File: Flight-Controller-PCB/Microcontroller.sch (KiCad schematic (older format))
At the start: 32 parts, among them J8 USB_B_Micro, J9 ICSP, SW1 Reset, U3 FT232RL, U4 ATmega328P-AU, U5 LM1117-5.0, Y1 16 MHz

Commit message: Deleted majority of unused components. Started schematic for new MCU
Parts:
- removed C10, C11, C18: 0.1uF 16V X7R 10%, Capacitor_SMD:C_0603_1608Metric_Pad1.05x0.95mm_HandSolder, symbol Device:C
- removed D2, D3: Orange 1.9V 20mA, LED_SMD:LED_0603_1608Metric_Pad1.05x0.95mm_HandSolder, symbol Device:LED
- removed D5: Green 2.2V 20mA, LED_SMD:LED_0603_1608Metric_Pad1.05x0.95mm_HandSolder, symbol Device:LED
- removed J9: ICSP, Connector_PinHeader_2.54mm:PinHeader_2x03_P2.54mm_Vertical, symbol Connector_Generic:Conn_02x03_Odd_Even
- removed R16, R17, R22: 200 ohm 5%, Resistor_SMD:R_0603_1608Metric_Pad1.05x0.95mm_HandSolder, symbol Device:R
- removed R21: 1 kohm 5%, Resistor_SMD:R_0603_1608Metric_Pad1.05x0.95mm_HandSolder, symbol Device:R
- removed SW1: Reset, Custom:Switch, symbol Custom:Push-Switch
- removed U3: FT232RL, Package_SO:SSOP-28_5.3x10.2mm_P0.65mm, symbol Interface_USB:FT232RL
- removed U4: ATmega328P-AU, Package_QFP:TQFP-32_7x7mm_P0.8mm, symbol MCU_Microchip_ATmega:ATmega328P-AU
- added R? (x2): 22 ohm 1%, Resistor_SMD:R_0603_1608Metric_Pad1.05x0.95mm_HandSolder, symbol Device:R
- added U?: ATmega32U4-AU, Package_QFP:TQFP-44_10x10mm_P0.8mm, symbol MCU_Microchip_ATmega:ATmega32U4-AU
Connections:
- net labels added: D+, D-
- net labels removed: +3.3V
- wire segments 131 -> 92
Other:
- note removed: "ICSP"
- moved on the sheet: C12, C7, C8, C9, F1, J8, R18, R19, Y1

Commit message: Learned a lot about crystals
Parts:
- added C?: 1uF 16V X7R 10%, Capacitor_SMD:C_0603_1608Metric_Pad1.05x0.95mm_HandSolder, symbol Device:C
- added C? (x2): 22pF 12V X7R 2%, Capacitor_SMD:C_0603_1608Metric_Pad1.05x0.95mm_HandSolder, symbol Device:C
- added Y?: 16MHz, CL 7pF, Custom:Crystal, symbol Device:Crystal
- U?: Digi-Key # (none) -> ATMEGA32U4RC-AU-ND; Digi-Key LinkDigi LinkDigi-Key Link (none) -> https://www.digikey.ca/en/products/detail/microchip-technol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; Manufacturer (none) -> Microchip Technology; Manufacturer # (none) -> ATMEGA32U4RC-AU
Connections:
- wire segments 92 -> 107
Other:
- note added: "CL= (CX1 * CX2)/(CX1 + CX2) + CSTRAY\nCL = (CX * CX)/(CX + CX) + CSTRAY <= substitute CX for CX1 and CX2 since they equal each other\nCL = (CX^2)/(2CX) + CSTRAY\nCL = (CX/2) + CSTRAY\nCL - CSTRAY = (CX/2)\n2*(CL -CSTRAY) = CX\n\nCX1 = CX2 = 2*(CL-CSTRAY)\n\nCSTRAY approx 4pF\n\n22/2 = 11 - 4 = 7 ish"
- note added: "https://blog.adafruit.com/2012/01/24/choosing-the-right-crystal-and-caps-for-your-design/\nC1, C2 = 2*CL – 2*Cstray\n\nhttps://forum.digikey.com/t/crystal-oscillator-load-cap-selection/1915\nC1, C2 = 2*(CL) - Cstray"
- note added: "load capacitance of crystal * 2 - stray cap pin and trace = cap size \nhttps://www.microchip.com/forums/m881105.aspx\nhttps://www.sparkfun.com/products/94"
- moved on the sheet: C12, C13, C14, C15, C16, C17, D4, F1, J8, R20, R?, U?

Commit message: Power Management and Selection roughed out
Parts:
- removed C13: 10uF 25V 20%, Capacitor_SMD:C_0603_1608Metric_Pad1.05x0.95mm_HandSolder, symbol Device:CP
- removed C15: 1uF 16V X7R 10%, Capacitor_SMD:C_0603_1608Metric_Pad1.05x0.95mm_HandSolder, symbol Device:C
- removed C16: 4.7uF 10V 20%, Capacitor_SMD:C_0603_1608Metric_Pad1.05x0.95mm_HandSolder, symbol Device:CP
- removed C17: 0.1uF 16V X7R 10%, Capacitor_SMD:C_0603_1608Metric_Pad1.05x0.95mm_HandSolder, symbol Device:C
- removed D4: Green 2.2V 20mA, LED_SMD:LED_0603_1608Metric_Pad1.05x0.95mm_HandSolder, symbol Device:LED
- removed D6: SS1P3L, Custom:SS1P3L, symbol Device:D_Schottky
- removed R20: 150 ohm 5%, Resistor_SMD:R_0603_1608Metric_Pad1.05x0.95mm_HandSolder, symbol Device:R
- removed U5: LM1117-5.0, Package_TO_SOT_SMD:SOT-223, symbol Custom:LM1117-5.0
- added C?: 1uF 16V X7R 10%, Capacitor_SMD:C_0603_1608Metric_Pad1.05x0.95mm_HandSolder, symbol Device:C
- added C? (x2): 0.1uF 20V X7R 10%, Capacitor_SMD:C_0603_1608Metric_Pad1.05x0.95mm_HandSolder, symbol Device:C
- added C?: 1uF 12V X7R 10%, Capacitor_SMD:C_0603_1608Metric_Pad1.05x0.95mm_HandSolder, symbol Device:C
- added Q? (x2): Q_PMOS_GSD, Package_TO_SOT_SMD:SOT-23, symbol Device:Q_PMOS_GSD
- added R?: 10 kohm 5%, Resistor_SMD:R_0603_1608Metric_Pad1.05x0.95mm_HandSolder, symbol Device:R
- added U?: NCP1117-5.0, Package_TO_SOT_SMD:SOT-223-3_TabPin2, symbol Regulator_Linear:NCP1117-5.0_SOT223
- added U?: LP2985-3.3, Package_TO_SOT_SMD:SOT-23-5, symbol Regulator_Linear:LP2985-3.3
- C15: renamed from C14; value 10uF 25V 20% -> 22uF 16V 20%
- gave numbers to parts that had none: 7
- renumbered C9 to C10, C7 to C8, C8 to C9, R18 to R16, R19 to R17, Y1 to Y2
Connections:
- net labels added: +3.3V
- wire segments 107 -> 110
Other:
- note added: "Power Management and Selection"
- note removed: "5V Regulation and Selection"
- moved on the sheet: C15

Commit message: USB interface
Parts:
- removed C?: 1uF 16V X7R 10%, Capacitor_SMD:C_0603_1608Metric_Pad1.05x0.95mm_HandSolder, symbol Device:C
- added C?: 22uF 10V 20%, Capacitor_SMD:C_0603_1608Metric_Pad1.05x0.95mm_HandSolder, symbol Device:CP
- added C?: 0.1uF 16V X7R 10%, Capacitor_SMD:C_0603_1608Metric_Pad1.05x0.95mm_HandSolder, symbol Device:C
- added R?: 10 kohm 5%, Resistor_SMD:R_0603_1608Metric_Pad1.05x0.95mm_HandSolder, symbol Device:R
- added RV? (x2): 5V 0.5pF, Diode_SMD:D_0603_1608Metric_Pad1.05x0.95mm_HandSolder, symbol Device:Varistor
- C?: value 0.1uF 20V X7R 10% -> 0.1uF 16V X7R 10%
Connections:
- wire segments 110 -> 126
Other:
- moved on the sheet: C15, C?, F1, J8, Q?, R19, R20, R?, U?

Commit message: Push before branch switch
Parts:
- removed Y2: 16 MHz, Custom:Resonator, symbol Device:Resonator
- added C? (x2): 0.1uF 16V X7R 10%, Capacitor_SMD:C_0603_1608Metric_Pad1.05x0.95mm_HandSolder, symbol Device:C
- added C?: 1uF 12V X7R 10%, Capacitor_SMD:C_0603_1608Metric_Pad1.05x0.95mm_HandSolder, symbol Device:C
- added C?: 0.1uF 20V X7R 10%, Capacitor_SMD:C_0603_1608Metric_Pad1.05x0.95mm_HandSolder, symbol Device:C
- added D?: D, symbol Device:D
- added FB?: Ferrite_Bead, symbol Device:Ferrite_Bead
- added R?: 10 kohm 5%, Resistor_SMD:R_0603_1608Metric_Pad1.05x0.95mm_HandSolder, symbol Device:R
- added SW?: Push-Switch, Custom:Switch, symbol Custom:Push-Switch
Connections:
- net labels added: A4, A5, D0_RX, D1_TX, D2_SDA, D3_SCL, D4_A6
- wire segments 126 -> 152
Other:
- moved on the sheet: C11, C12, C13, C7, U3, Y1

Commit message: Mostly finished off the schematic, need to double check and label
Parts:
- removed C10, C8: 1uF 16V X7R 10%, Capacitor_SMD:C_0603_1608Metric_Pad1.05x0.95mm_HandSolder, symbol Device:C
- removed C9: 4.7uF 10V 20%, Capacitor_SMD:C_0603_1608Metric_Pad1.05x0.95mm_HandSolder, symbol Device:CP
- removed C?: 0.1uF 20V X7R 10%, Capacitor_SMD:C_0603_1608Metric_Pad1.05x0.95mm_HandSolder, symbol Device:C
- removed R16, R17: 1 kohm 5%, Resistor_SMD:R_0603_1608Metric_Pad1.05x0.95mm_HandSolder, symbol Device:R
- added C?: 1uF 12V X7R 10%, Capacitor_SMD:C_0603_1608Metric_Pad1.05x0.95mm_HandSolder, symbol Device:C
- added R?: 10 kohm, Resistor_SMD:R_0603_1608Metric_Pad1.05x0.95mm_HandSolder, symbol Device:R
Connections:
- net labels added: MISO, MOSI, SCK, SCL, SDA
- net labels removed: A4_SDA, A5_SCL, A6, A7, D0_RX, D1_TX, D2, D2_SDA, D3, D3_SCL, D4_A6
- wire segments 152 -> 136
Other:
- note added: "A0"
- note added: "A1"
- note added: "A10"
- note added: "A2"
- note added: "A3"
- note added: "A4"
- note added: "A5"
- note added: "A6"
- note added: "A7"
- note added: "A8"
- note added: "D0"
- note added: "D1"
- note added: "D10"
- note added: "D11"
- note added: "D13"
- note added: "D14"
- note added: "D15"
- note added: "D16"
- note added: "D2"
- note added: "D3"
- note added: "D5"
- note added: "D7"
- note added: "D8"
- note removed: "CL= (CX1 * CX2)/(CX1 + CX2) + CSTRAY\nCL = (CX * CX)/(CX + CX) + CSTRAY <= substitute CX for CX1 and CX2 since they equal each other\nCL = (CX^2)/(2CX) + CSTRAY\nCL = (CX/2) + CSTRAY\nCL - CSTRAY = (CX/2)\n2*(CL -CSTRAY) = CX\n\nCX1 = CX2 = 2*(CL-CSTRAY)\n\nCSTRAY approx 4pF\n\n22/2 = 11 - 4 = 7 ish"
- note removed: "https://blog.adafruit.com/2012/01/24/choosing-the-right-crystal-and-caps-for-your-design/\nC1, C2 = 2*CL – 2*Cstray\n\nhttps://forum.digikey.com/t/crystal-oscillator-load-cap-selection/1915\nC1, C2 = 2*(CL) - Cstray"
- note removed: "load capacitance of crystal * 2 - stray cap pin and trace = cap size \nhttps://www.microchip.com/forums/m881105.aspx\nhttps://www.sparkfun.com/products/94"
- moved on the sheet: C11, C12, C13, C15, C7, C?, D?, F1, FB?, J8, Q?, R19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

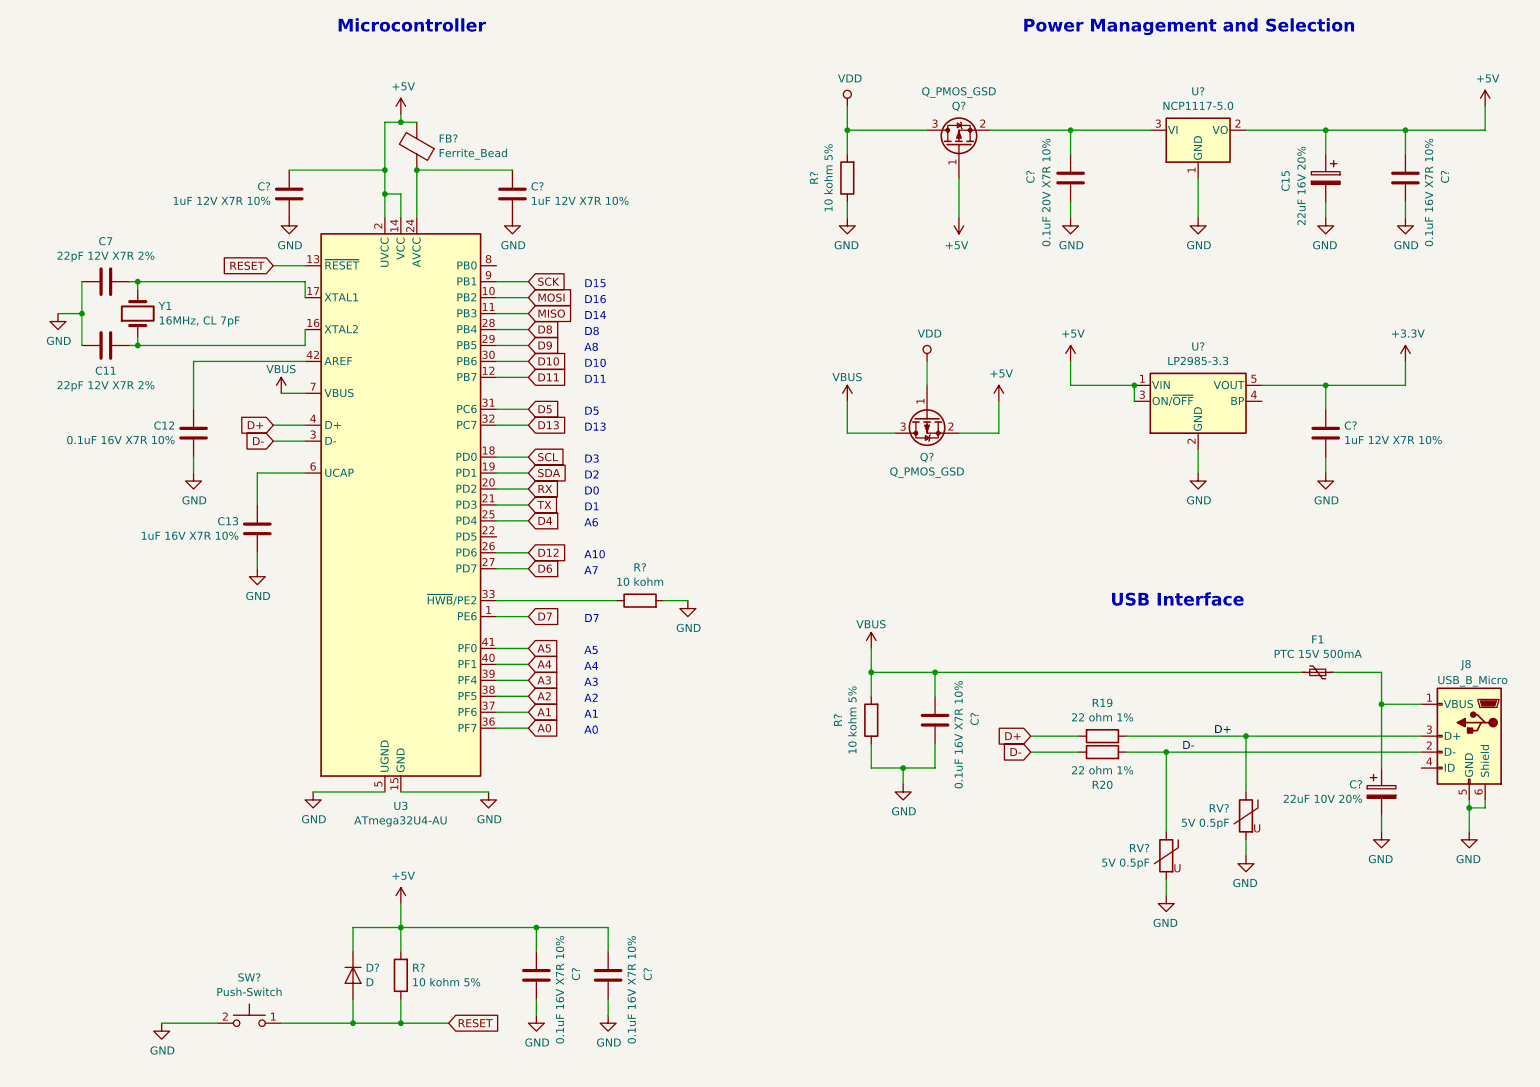
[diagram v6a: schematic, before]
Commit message: Updated pin mappings
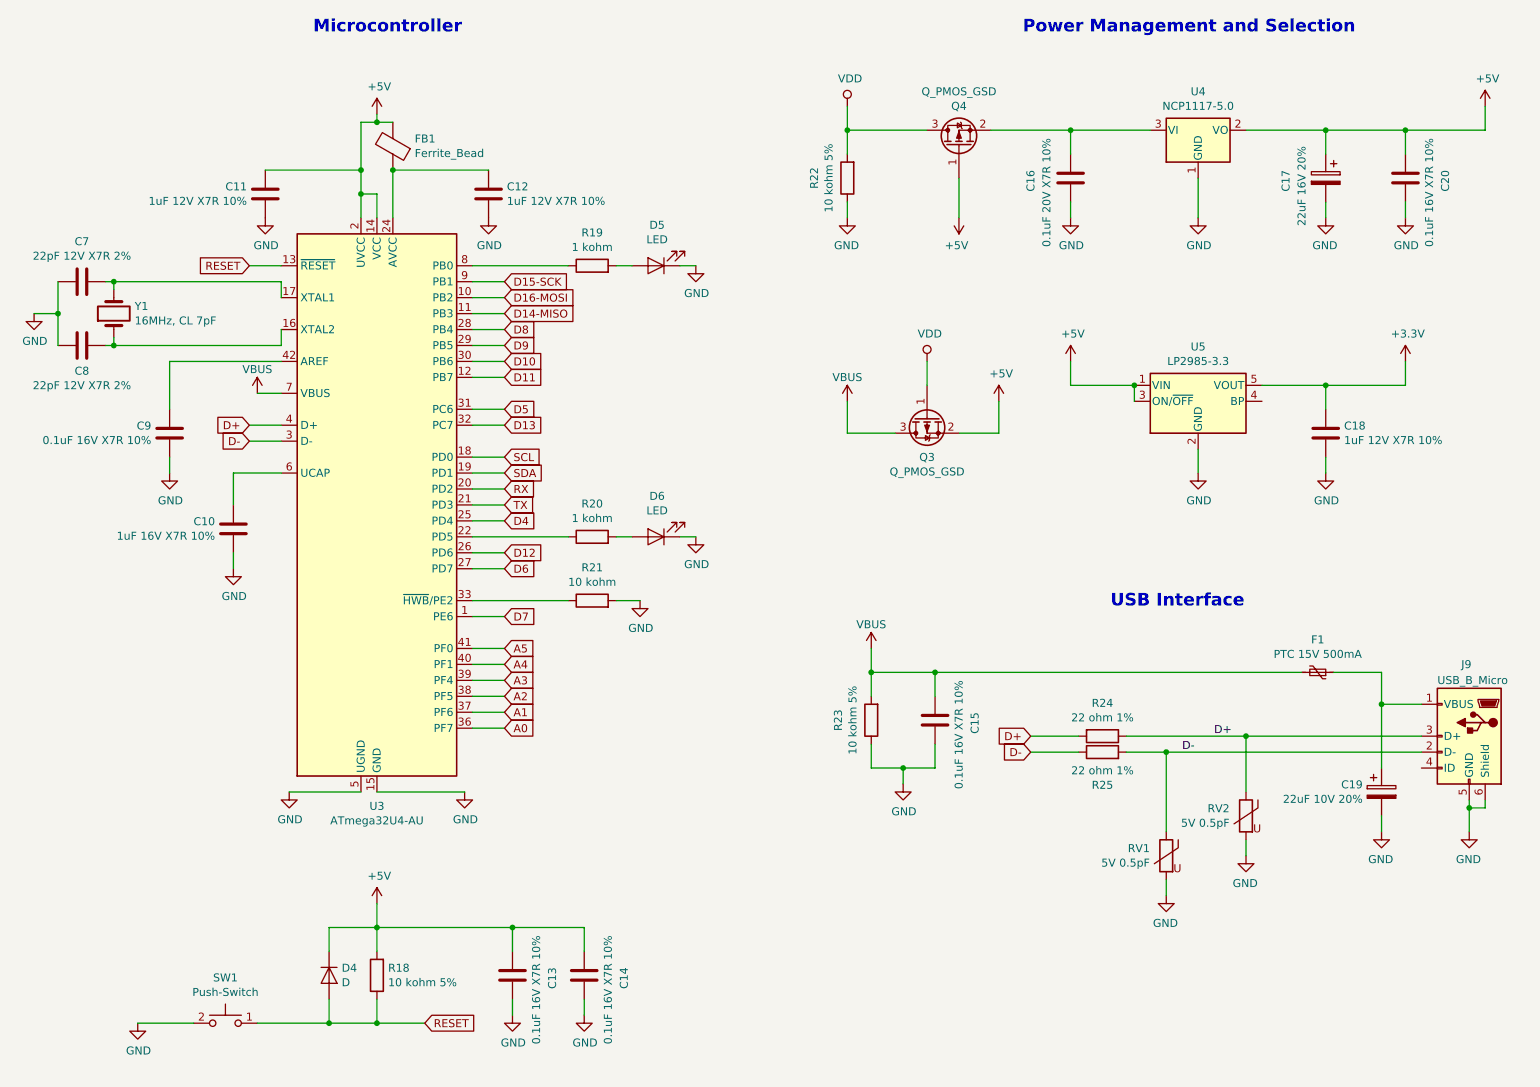
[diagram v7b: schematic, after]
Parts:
- added D5, D6: LED, LED_SMD:LED_0603_1608Metric_Pad1.05x0.95mm_HandSolder, symbol Device:LED
- added R19, R20: 1 kohm, Resistor_SMD:R_0603_1608Metric_Pad1.05x0.95mm_HandSolder, symbol Device:R
- gave numbers to parts that had none: 22
- renumbered C13 to C10, C15 to C17, C11 to C8, C12 to C9, J8 to J9, R19 to R24, R20 to R25
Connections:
- net GND: now also D5.1 (K), D6.1 (K)
- net at U3.22 (PD5): now also R20.1
- net at U3.8 (PB0): now also R19.1
- net MISO renamed D14-MISO
- net MOSI renamed D16-MOSI
- net SCK renamed D15-SCK
- new net: D6.2 (A), R20.2
- new net: D5.2 (A), R19.2
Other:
- note removed: "A0"
- note removed: "A1"
- note removed: "A10"
- note removed: "A2"
- note removed: "A3"
- note removed: "A4"
- note removed: "A5"
- note removed: "A6"
- note removed: "A7"
- note removed: "A8"
- note removed: "D0"
- note removed: "D1"
- note removed: "D10"
- note removed: "D11"
- note removed: "D13"
- note removed: "D14"
- note removed: "D15"
- note removed: "D16"
- note removed: "D2"
- note removed: "D3"
- note removed: "D5"
- note removed: "D7"
- note removed: "D8"
- moved on the sheet: C10, C11, C12, C13, C14, C7, C8, C9, D4, FB1, R18, R21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
